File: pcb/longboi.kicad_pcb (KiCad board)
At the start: 4 copper layers, 358 x 40 mm, 285 parts, among them J1 Testpad, J10 Conn_01x04_Pin, J11 Conn_01x02_Pin, J12 Conn_01x02_Pin, J13 Conn_01x02_Pin, J14 Conn_01x02_Pin, J15 Conn_01x03_Pin, J16 Conn_01x03_Pin, J17 Conn_01x03_Pin, J18 Conn_01x03_Pin, J19 Conn_01x02_Pin, J2 Testpad, J20 MX3.0, J21 MX3.0, J23 JST-XH, J24 JST-XH, J25 JST-XH, J26 JST-XH, J27 JST-XH, J28 JST-XH, J29 JST-XH, J3 Testpad, J30 JST-XH, J31 JST-XH, J32 JST-XH, J33 JST-XH, J34 JST-XH, J35 JST-XH, J36 JST-XH, J37 JST-XH, J38 JST-XH, J39 Conn_01x02_Pin, J4 Testpad, J40 Conn_01x03_Pin, J41 Conn_01x02_Pin, J42 JST-ZH, J44 Conn_01x02_Pin, J5 Testpad, J50 Conn_01x02_Pin, J6 JST-ZH, J7 Conn_01x04_Pin, J8 Conn_01x04_Pin, J9 Conn_01x04_Pin, Q1 HY1904C2, Q2 IRLML0030, Q4 IRLML0030, SW1 SW_SPST, SW2 SW_SPST, U1 STM32H723VGTx, U10 DRV8837, U11 DRV8837, U12 74LVC1G126, U13 74LVC1G126, U14 74LVC1G126, U15 74LVC1G126, U16 SN65HVD231, U17 TPS2116DRL, U18 TPS56637RPAR, U19 ME6211C33M5, U2 SN74LVC245APW, U20 SMF05CT1G-ES, U21 74LVC1G126, U22 74LVC1G126, U3 SN74LVC245APW, U4 TMC2209-LA, U5 TMC2209-LA, U6 TMC2209-LA, U7 TMC2209-LA, U8 DRV8837, U9 DRV8837, Y1 Crystal_GND24

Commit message: update pcb
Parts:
- removed REF** (x7): MountingHole_3.2mm_M3_DIN965_Pad, MountingHole:MountingHole_3.2mm_M3_DIN965_Pad
- C3, C6: value 12pF -> 20pF
- C57, C59: value 1uF -> 10uF
- R1, R24, R64, R70: value 1k -> 2.7k
- R14: value 12k -> 56k
- R18: value 1k -> 3.3k
- R25, R61, R79, R80, R81, R82, R83, R84, R85, R86, R87, R88, R89, R90, R91, R92, R93, R94: value 1.5k -> 3.3k

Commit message: fixes #9 fixes #4 fixes #13
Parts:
- added U23: SMF05CT1G-ES, Package_TO_SOT_SMD:SOT-363_SC-70-6, F.Cu at (57.0, 105.3)
- F1: footprint Fuse:Fuseholder_Littelfuse_Nano2_157x -> Fuse:Fuseholder_Littelfuse_Nano2_154x
- moved U16 2.46 mm to (71.8, 105.5)
- moved C52 2.45 mm to (76.4, 105.5)
- moved J19 2.45 mm to (64.0, 104.0)
- moved R12 2.45 mm to (66.6, 103.7)
- moved F1 1.57 mm to (40.2, 113.0)
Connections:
- F1 pad 1: Net-(J20-Pin_2) -> Net-(J20-Pin_1)
- J19 pad 2: Net-(J19-Pin_2) -> /24V_CAN/CANH
- J20 pad 1: GND -> Net-(J20-Pin_1)
- J20 pad 2: Net-(J20-Pin_2) -> GND
- J20 pad 3: Net-(J20-Pin_3) -> /24V_CAN/CANH
- J20 pad 4: Net-(J19-Pin_2) -> /24V_CAN/CANL
- J21 pad 1: GND -> Net-(J20-Pin_1)
- J21 pad 2: Net-(J20-Pin_2) -> GND
- J21 pad 3: Net-(J20-Pin_3) -> /24V_CAN/CANH
- J21 pad 4: Net-(J19-Pin_2) -> /24V_CAN/CANL
- R12 pad 1: Net-(J20-Pin_3) -> /24V_CAN/CANL
- U16 pad 6: Net-(J20-Pin_3) -> /24V_CAN/CANL
- U16 pad 7: Net-(J19-Pin_2) -> /24V_CAN/CANH
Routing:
- net /24V_CAN/CANH: track 0.00 -> 367.4 mm
- net Net-(J19-Pin_2): track 353.0 -> 0.00 mm
- net /24V_CAN/CANL: track 0.00 -> 343.3 mm
- net Net-(J20-Pin_3): track 338.6 -> 0.00 mm
- net CAN_RX: track 160.8 -> 158.3 mm
- net GND: track 221.7 -> 223.9 mm, vias 153 -> 161
- net CAN_TX: track 164.5 -> 163.7 mm
- net +24V: vias 109 -> 94
- added copper zone on In1.Cu, net /24V_CAN/CANH
- added copper zone on F.Cu, net Net-(J20-Pin_1)
- removed copper zone on F.Cu, net Net-(J20-Pin_2)
- removed copper zone on In1.Cu, net Net-(J20-Pin_2)

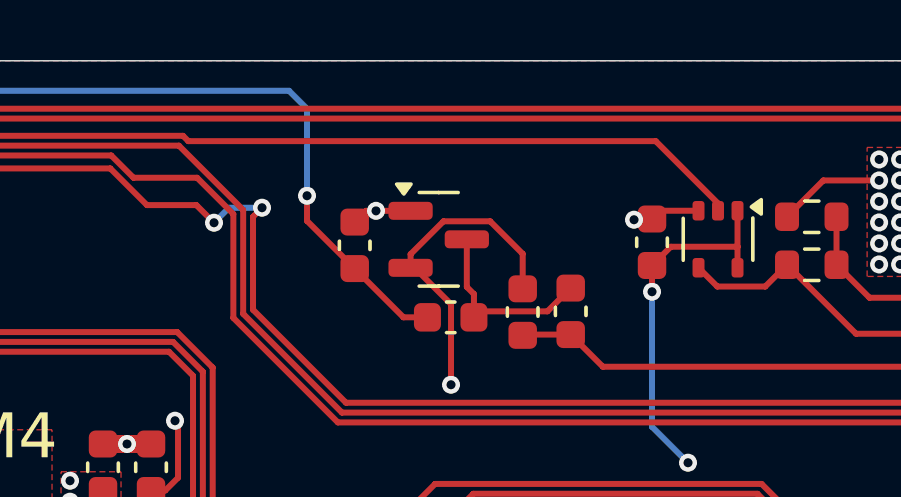
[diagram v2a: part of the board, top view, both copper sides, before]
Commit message: fixes #6
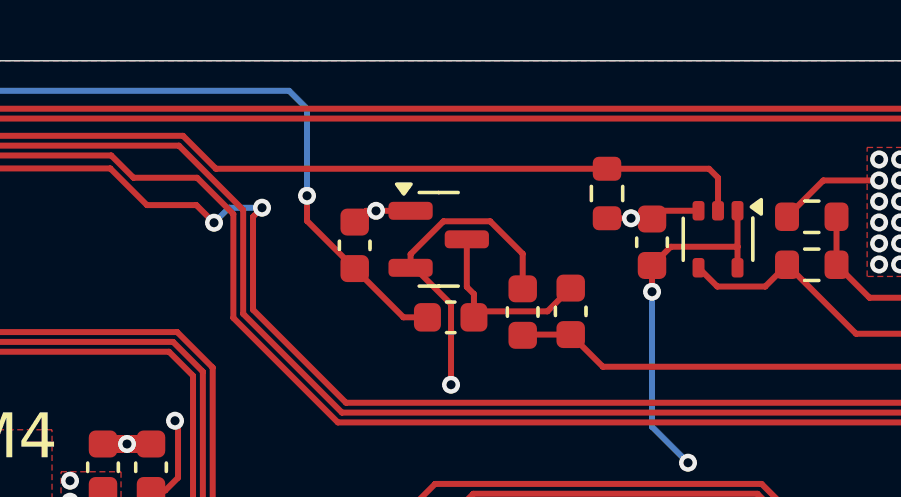
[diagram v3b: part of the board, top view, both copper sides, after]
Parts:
- added R20: 10k, Resistor_SMD:R_0603_1608Metric, F.Cu at (344.4, 103.4)
- R63, R66, R72: value 100k -> 10k
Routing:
- net GND: track 223.9 -> 224.8 mm
- net OUT1: track 135.8 -> 136.3 mm
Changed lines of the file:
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@@
 		)
 		(property "Value" "100nF"
-			(at 0 1.43 90)
+			(at 0 1.3 90)
 			(layer "F.Fab")
 			(effects
@@
 		)
 	)
+	(footprint "Resistor_SMD:R_0603_1608Metric"
+		(layer "F.Cu")
+		(at 344.4 103.425 -90)
+		(descr "Resistor SMD 0603 (1608 Metric), square (rectangular) end terminal, IPC-7351 nominal, (Body size source: IPC-SM-782 page 72, https://www.pcb-3d.com/wordpress/wp-content/uploads/ipc-sm-782a_amendment_1_and_2.pdf), generated with kicad-footprint-generator")
+		(tags "resistor")
+		(property "Reference" "R20"
+			(at 0 -1.43 90)
+			(layer "F.SilkS")
+			(hide yes)
+			(effects
+				(font
+					(size 1 1)
+					(thickness 0.15)
+				)
+			)
+		)
+		(property "Value" "10k"
+			(at 0 1.43 90)
+			(layer "F.Fab")
+			(effects
+				(font
+					(size 1 1)
+					(thickness 0.15)
+				)
+			)
+		)
+		(property "Datasheet" "~"
+			(at 0 0 90)
+			(layer "F.Fab")
+			(hide yes)
+			(effects
+				(font
+					(size 1.27 1.27)
+					(thickness 0.15)
+				)
+			)
+		)
+		(property "Description" "Resistor, small symbol"
+			(at 0 0 90)
+			(layer "F.Fab")
+			(hide yes)
+			(effects
+				(font
+					(size 1.27 1.27)
+					(thickness 0.15)
+				)
+			)
+		)
+		(property ki_fp_filters "R_*")
+		(sheetname "/Outputs/")
+		(sheetfile "outputs.kicad_sch")
+		(attr smd)
+		(fp_line
+			(start -0.237258 0.5225)
+			(end 0.237258 0.5225)
+			(stroke
+				(width 0.12)
+				(type solid)
+			)
+			(layer "F.SilkS")
+		)
+		(fp_line
+			(start -0.237258 -0.5225)
+			(end 0.237258 -0.5225)
+			(stroke
+				(width 0.12)
+				(type solid)
+			)
+			(layer "F.SilkS")
+		)
+		(fp_line
+			(start -1.48 0.73)
+			(end -1.48 -0.73)
+			(stroke
+				(width 0.05)
+				(type solid)
+			)
+			(layer "F.CrtYd")
+		)
+		(fp_line
+			(start 1.48 0.73)
+			(end -1.48 0.73)
+			(stroke
+				(width 0.05)
+				(type solid)
+			)
+			(layer "F.CrtYd")
+		)
+		(fp_line
+			(start -1.48 -0.73)
+			(end 1.48 -0.73)
+			(stroke
+				(width 0.05)
+				(type solid)
+			)
+			(layer "F.CrtYd")
+		)
+		(fp_line
+			(start 1.48 -0.73)
+			(end 1.48 0.73)
+			(stroke
+				(width 0.05)
+				(type solid)
+			)
+			(layer "F.CrtYd")
+		)
+		(fp_line
+			(start -0.8 0.4125)
+			(end -0.8 -0.4125)
+			(stroke
+				(width 0.1)
+				(type solid)
+			)
+			(layer "F.Fab")
+		)
+		(fp_line
+			(start 0.8 0.4125)
+			(end -0.8 0.4125)
+			(stroke
+				(width 0.1)
+				(type solid)
+			)
+			(layer "F.Fab")
+		)
+		(fp_line
+			(start -0.8 -0.4125)
+			(end 0.8 -0.4125)
+			(stroke
+				(width 0.1)
+				(type solid)
+			)
+			(layer "F.Fab")
+		)
+		(fp_line
+			(start 0.8 -0.4125)
+			(end 0.8 0.4125)
+			(stroke
+				(width 0.1)
+				(type solid)
+			)
+			(layer "F.Fab")
+		)
+		(fp_text user "${REFERENCE}"
+			(at 0 0 90)
+			(layer "F.Fab")
+			(effects
+				(font
+					(size 0.4 0.4)
+					(thickness 0.06)
+				)
+			)
+		)
+		(pad "1" smd roundrect
+			(at -0.825 0 270)
+			(size 0.8 0.95)
+			(layers "F.Cu" "F.Mask" "F.Paste")
+			(roundrect_rratio 0.25)
+			(net 198 "OUT1")
+			(pintype "passive")
+		)
+		(pad "2" smd roundrect
+			(at 0.825 0 270)
+			(size 0.8 0.95)
+			(layers "F.Cu" "F.Mask" "F.Paste")
+			(roundrect_rratio 0.25)
+			(net 1 "GND")
+			(pintype "passive")
+		)
+		(embedded_fonts no)
+		(model "${KICAD9_3DMODEL_DIR}/Resistor_SMD.3dshapes/R_0603_1608Metric.step"
+			(offset
+				(xyz 0 0 0)
+			)
+			(scale
+				(xyz 1 1 1)
+			)
+			(rotate
+				(xyz 0 0 0)
+			)
+		)
+	)
 	(footprint "Connector_JST:JST_XH_B3B-XH-A_1x03_P2.50mm_Vertical"
 		(locked yes)
@@
 			)
 		)
-		(property "Value" "100k"
+		(property "Value" "10k"
 			(at 0 1.43 90)
 			(layer "F.Fab")
@@
 			)
 		)
-		(property "Value" "100k"
+		(property "Value" "10k"
 			(at 0 1.43 0)
 			(layer "F.Fab")
@@
 			)
 		)
-		(property "Value" "100k"
+		(property "Value" "10k"
 			(at 0 1.43 90)
 			(layer "F.Fab")
@@
 	)
 	(segment
+		(start 345.2 104.25)
+		(end 345.875 104.25)
+		(width 0.2)
+		(layer "F.Cu")
+		(net 1)
+	)
+	(segment
 		(start 256.7 113.3)
 		(end 256.7 115.5)
@@
 	)
 	(segment
+		(start 345.875 104.25)
+		(end 345.9 104.275)
+		(width 0.2)
+		(layer "F.Cu")
+		(net 1)
+	)
+	(segment
 		(start 58.649 130.326)
 		(end 59.4 129.575)
@@
 	)
 	(segment
-		(start 345.325 104.275)
-		(end 345.3 104.3)
-		(width 0.2)
-		(layer "F.Cu")
-		(net 1)
-	)
-	(segment
 		(start 224.2 123.9)
 		(end 224.775 123.325)
@@
 	)
 	(segment
+		(start 344.4 104.25)
+		(end 345.2 104.25)
+		(width 0.2)
+		(layer "F.Cu")
+		(net 1)
+	)
+	(segment
 		(start 123.3 114.65)
 		(end 123.35 114.6)
@@
 	)
 	(segment
-		(start 345.9 104.275)
-		(end 345.325 104.275)
-		(width 0.2)
-		(layer "F.Cu")
-		(net 1)
-	)
-	(segment
 		(start 259.6625 111.275)
 		(end 258.725 111.275)
@@
 	)
 	(via
-		(at 345.3 104.3)
-		(size 0.6)
-		(drill 0.3)
-		(layers "F.Cu" "B.Cu")
-		(net 1)
-	)
-	(via
 		(at 185.6 135.2)
 		(size 0.6)
@@
 		(net 1)
 	)
+	(via
+		(at 345.2 104.25)
+		(size 0.6)
+		(drill 0.3)
+		(layers "F.Cu" "B.Cu")
+		(net 1)
+	)
 	(segment
 		(start 67.555 111.155)
@@
 	)
 	(segment
-		(start 218.649 108.767176)
-		(end 218.649 109.601)
+		(start 347.8 102.6)
+		(end 348.1 102.9)
 		(width 0.2)
 		(layer "F.Cu")
@@
 	)
 	(segment
-		(start 330.443862 101.68)
-		(end 330.265862 101.502)
+		(start 218.649 108.767176)
+		(end 218.649 109.601)
 		(width 0.2)
 		(layer "F.Cu")
@@
 	)
 	(segment
-		(start 223.670276 101.502)
-		(end 330.265862 101.502)
+		(start 330.265862 101.502)
+		(end 331.363862 102.6)
 		(width 0.2)
 		(layer "F.Cu")
@@
 	)
 	(segment
-		(start 348.1 103.75513)
-		(end 346.02487 101.68)
+		(start 344.4 102.6)
+		(end 347.8 102.6)
 		(width 0.2)
 		(layer "F.Cu")
@@
 	)
 	(segment
-		(start 218.649 108.767176)
-		(end 218.944 108.472176)
+		(start 223.670276 101.502)
+		(end 330.265862 101.502)
 		(width 0.2)
 		(layer "F.Cu")
@@
 	)
 	(segment
-		(start 346.02487 101.68)
-		(end 330.443862 101.68)
+		(start 331.363862 102.6)
+		(end 344.4 102.6)
 		(width 0.2)
 		(layer "F.Cu")
@@
 	)
 	(segment
-		(start 348.1 104)
-		(end 348.1 103.75513)
+		(start 348.1 102.9)
+		(end 348.1 104)
+		(width 0.2)
+		(layer "F.Cu")
+		(net 198)
+	)
+	(segment
+		(start 218.649 108.767176)
+		(end 218.944 108.472176)
 		(width 0.2)
 		(layer "F.Cu")
